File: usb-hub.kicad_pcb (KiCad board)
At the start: 4 copper layers, 50 x 100 mm, 151 parts, among them IC101 USB2517, J101 Barrel_Jack, J102 USB_C_Receptacle_USB2.0_14P, J201 USB_A, J202 USB_A, J301 USB_A, J302 USB_A, J401 USB_A, J402 USB_A, J601 Prog, SW201 SW_Push, SW202 SW_Push, SW301 SW_Push, SW302 SW_Push, SW401 SW_Push, SW402 SW_Push, U101 SRV05-4, U201 MIC2026-1xM, U202 SRV05-4, U203 74LVC2G08, U301 MIC2026-1xM, U302 SRV05-4, U303 74LVC2G08, U401 MIC2026-1xM, U402 SRV05-4, U403 74LVC2G08, U501 TPS54331, U502 TPS54331, U601 STM32L151C8Tx, Y101 24Mhz

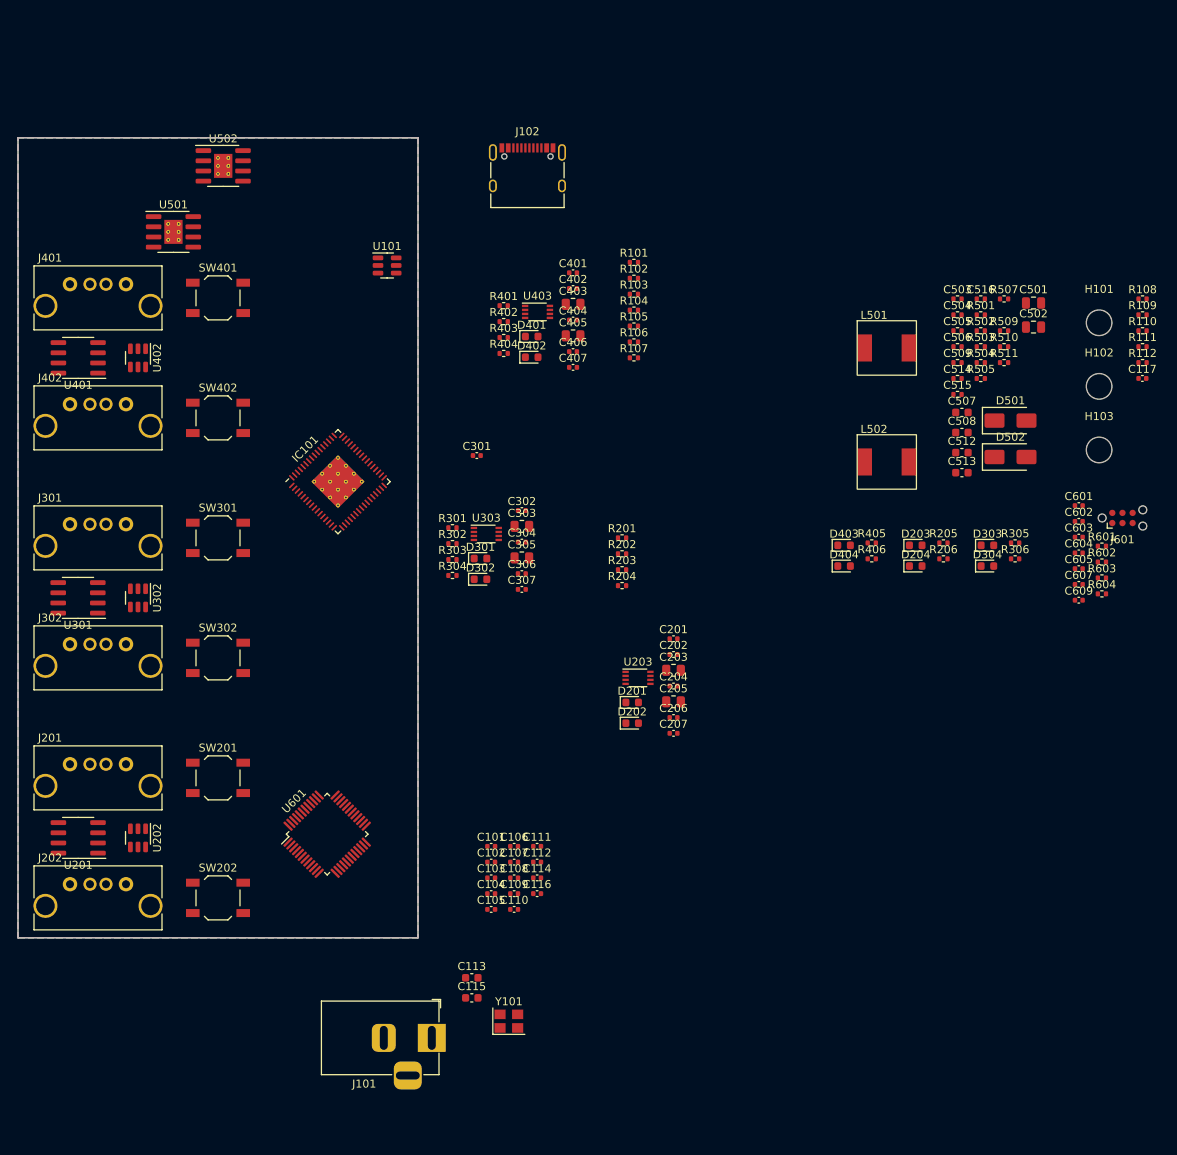
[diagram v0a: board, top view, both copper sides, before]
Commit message: Refine connectors and overall shape
Replace USB connectors, because of availability.
Use available barrel jack and USB-C connector instead of generic ones.
Update 3D Models

Refine rough placement of parts and board outline
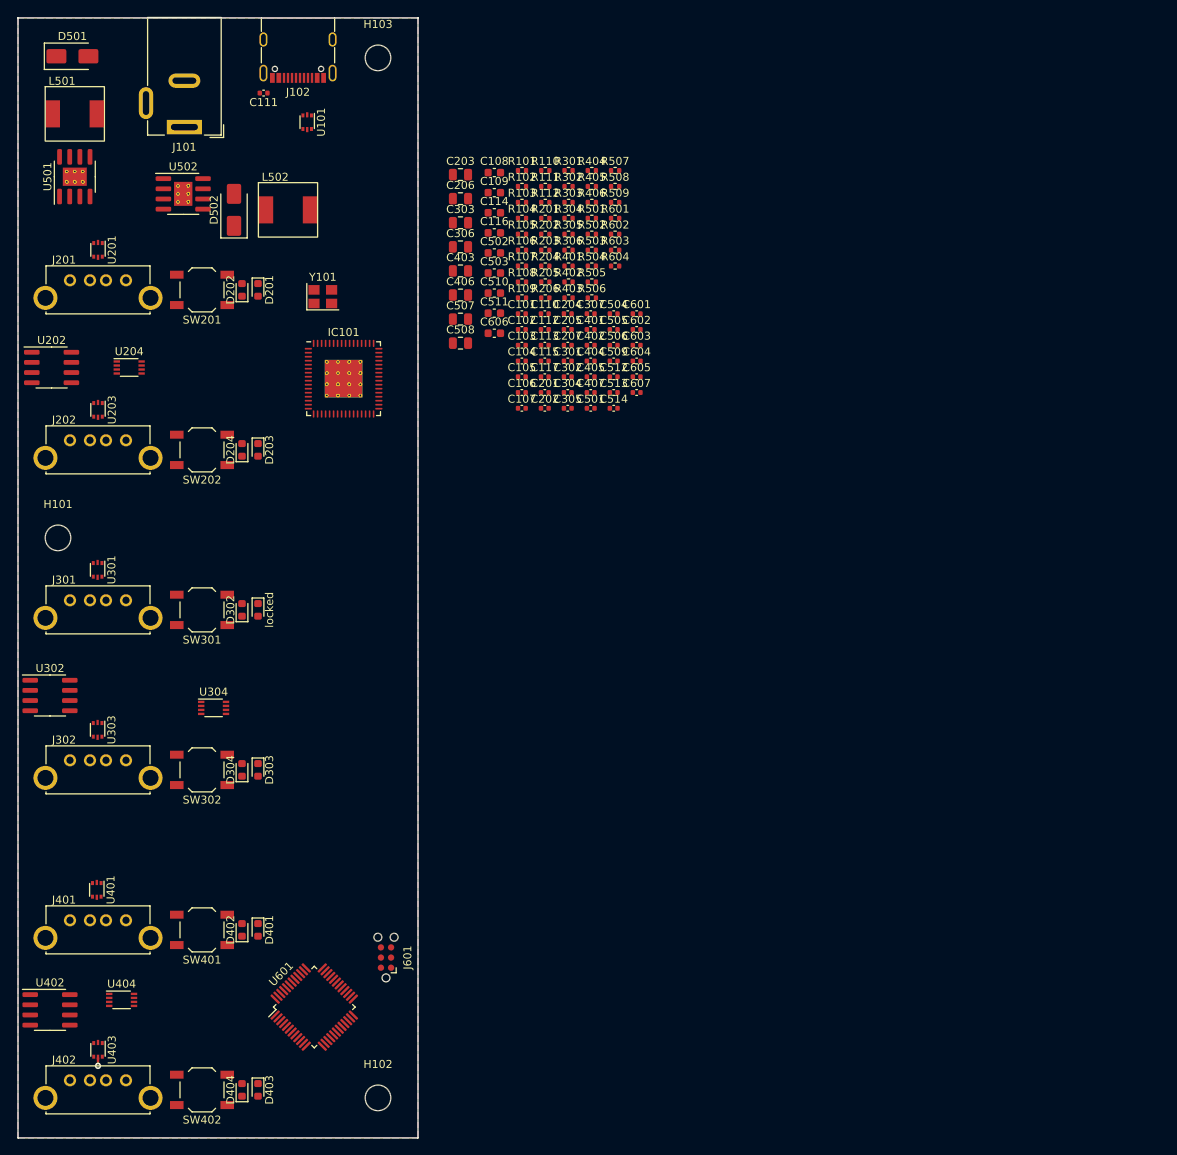
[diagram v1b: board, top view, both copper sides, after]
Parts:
- removed C515: 1nF, Resistor_SMD:R_0402_1005Metric
- removed C516: 47pF, Resistor_SMD:R_0402_1005Metric
- removed C609: 1.0uF, Capacitor_SMD:C_0402_1005Metric
- removed R510: 29,4k, Resistor_SMD:R_0402_1005Metric
- removed R511: 1,5k, Resistor_SMD:R_0402_1005Metric
- added C510: 22uF, Capacitor_SMD:C_0603_1608Metric, F.Cu at (159.5, 69.4)
- added C511: 22uF, Capacitor_SMD:C_0603_1608Metric, F.Cu at (159.5, 71.9)
- added C606: 1.0uF, Capacitor_SMD:C_0603_1608Metric, F.Cu at (159.5, 74.4)
- added R506: 220k, Resistor_SMD:R_0402_1005Metric, F.Cu at (171.7, 70.0)
- added R508: 3,3k, Resistor_SMD:R_0402_1005Metric, F.Cu at (174.6, 56.1)
- added U204: 74LVC2G08, Package_SO:VSSOP-8_2.3x2mm_P0.5mm, F.Cu at (113.9, 78.7)
- added U304: 74LVC2G08, Package_SO:VSSOP-8_2.3x2mm_P0.5mm, F.Cu at (124.5, 121.2)
- added U404: 74LVC2G08, Package_SO:VSSOP-8_2.3x2mm_P0.5mm, F.Cu at (113.0, 157.8)
- C108, C109: footprint Capacitor_SMD:C_0402_1005Metric -> Capacitor_SMD:C_0603_1608Metric
- C111: value C -> 100nF
- C113: value 1.0uF -> C; footprint Capacitor_SMD:C_0603_1608Metric -> Capacitor_SMD:C_0402_1005Metric
- C114, C116: value 100nF -> 1.0uF; footprint Capacitor_SMD:C_0402_1005Metric -> Capacitor_SMD:C_0603_1608Metric
- C115: value 1.0uF -> 100nF; footprint Capacitor_SMD:C_0603_1608Metric -> Capacitor_SMD:C_0402_1005Metric
- C203, C303, C403: footprint Resistor_SMD:R_0805_2012Metric -> Capacitor_SMD:C_0805_2012Metric
- C205, C305, C405: value 47uF -> 100nF; footprint Resistor_SMD:R_0805_2012Metric -> Capacitor_SMD:C_0402_1005Metric
- C206, C306, C406: value 100nF -> 47uF; footprint Capacitor_SMD:C_0402_1005Metric -> Capacitor_SMD:C_0805_2012Metric
- C501: value 10uF -> 100nF; footprint Capacitor_SMD:C_0805_2012Metric -> Capacitor_SMD:C_0402_1005Metric
- C502: value 10uF -> 22uF; footprint Capacitor_SMD:C_0805_2012Metric -> Capacitor_SMD:C_0603_1608Metric
- C503: value 10nF -> 22uF; footprint Resistor_SMD:R_0402_1005Metric -> Capacitor_SMD:C_0603_1608Metric
- C504: value 1nF -> 10nF; footprint Resistor_SMD:R_0402_1005Metric -> Capacitor_SMD:C_0402_1005Metric
- C505: value 47pF -> 1nF; footprint Resistor_SMD:R_0402_1005Metric -> Capacitor_SMD:C_0402_1005Metric
- C506: value 100nF -> 47pF; footprint Resistor_SMD:R_0402_1005Metric -> Capacitor_SMD:C_0402_1005Metric
- C507, C508: value 22uF -> 10uF; footprint Capacitor_SMD:C_0603_1608Metric -> Capacitor_SMD:C_0805_2012Metric
- C509: footprint Resistor_SMD:R_0402_1005Metric -> Capacitor_SMD:C_0402_1005Metric
- C512: value 22uF -> 10nF; footprint Capacitor_SMD:C_0603_1608Metric -> Capacitor_SMD:C_0402_1005Metric
- C513: value 22uF -> 1nF; footprint Capacitor_SMD:C_0603_1608Metric -> Capacitor_SMD:C_0402_1005Metric
- C514: value 10nF -> 47pF; footprint Resistor_SMD:R_0402_1005Metric -> Capacitor_SMD:C_0402_1005Metric
- D201, D203, D303, D401, D403: value LED -> GREEN
- D202, D204, D302, D304, D402, D404: value LED -> BLUE
- J101: value Barrel_Jack -> Barrel_Jack_Switch; footprint Connector_BarrelJack:BarrelJack_Horizontal -> Connector_BarrelJack:BarrelJack_Wuerth_6941xx301002
- J102: footprint Connector_USB:USB_C_Receptacle_XKB_U262-16XN-4BVC11 -> Connector_USB:USB_C_Receptacle_G-Switch_GT-USB-7010ASV
- J201, J202, J301, J302, J401, J402: footprint Connectors:CU01SAV1S00 -> Connectors:UJ2-AV-W4-TH
- R104, R105: value 5.1k -> 100k
- R106: value 1M -> 100k
- R107: value 12k -> 5.1k
- R108: value 100k -> 5.1k
- R110: value 100k -> 1M
- R111: value 100k -> 12k
- R203, R303, R403: value 1k -> 330
- R204, R304, R404: value 100k -> 1k
- R205, R305, R405: value 330 -> 100k
- R501: value 470k -> 10k
- R502: value 220k -> 1,5k
- R503: value 29,4k -> 33k
- R504: value 10k -> 330R
- R505: value 330R -> 470k
- R509: value 3,3k -> 33k
- R602: value 100k -> 10K
- R604: value 10K -> 100k
- U101: value SRV05-4 -> USBLC6-2P6; footprint Package_TO_SOT_SMD:SOT-23-6 -> Package_TO_SOT_SMD:SOT-666
- U201, U301, U401: value MIC2026-1xM -> USBLC6-2P6; footprint Package_SO:SOIC-8_3.9x4.9mm_P1.27mm -> Package_TO_SOT_SMD:SOT-666
- U202, U302, U402: value SRV05-4 -> MIC2026-1xM; footprint Package_TO_SOT_SMD:SOT-23-6 -> Package_SO:SOIC-8_3.9x4.9mm_P1.27mm
- U203, U303, U403: value 74LVC2G08 -> USBLC6-2P6; footprint Package_SO:VSSOP-8_2.3x2mm_P0.5mm -> Package_TO_SOT_SMD:SOT-666
- locked: renamed from D301; value LED -> GREEN
- moved H101 132.9 mm to (105.0, 100.0)
- moved H102 126.6 mm to (145.0, 170.0)
- moved D501 125.8 mm to (106.8, 39.8)
- moved J101 118.0 mm to (120.8, 48.6), turned to 180 degrees
- moved U403 107.4 mm to (110.0, 164.0), turned to -90 degrees
- moved J601 107.2 mm to (146.0, 152.5), turned to 90 degrees
- moved L501 105.6 mm to (107.1, 47.0)
- moved H103 102.6 mm to (145.0, 40.0)
- moved D502 101.9 mm to (127.0, 59.0), turned to 90 degrees
- moved C111 100.2 mm to (130.7, 44.4), turned to 180 degrees
- moved D403 100.0 mm to (130.0, 169.0), turned to -90 degrees
- moved D404 99.8 mm to (128.0, 169.0), turned to 90 degrees
- moved D304 96.6 mm to (128.0, 129.0), turned to 90 degrees
- moved D303 95.4 mm to (130.0, 129.0), turned to -90 degrees
- moved Y101 93.5 mm to (138.1, 69.8)
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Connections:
- C111 pad 1: /XTAL_IN -> GND
- C111 pad 2: GND -> Earth
- C112 pad 1: /XTAL_OUT -> /XTAL_IN
- C113 pad 1: Net-(IC101-VDD18) -> /XTAL_OUT
- C115 pad 1: Net-(IC101-VDD18PLL) -> Net-(IC101-VDD18)
- C117 pad 1: GND -> Net-(IC101-VDD18PLL)
- C117 pad 2: Earth -> GND
- C204 pad 1: /Port 1-2/VBUS_B -> GND
- C204 pad 2: GND -> Earth
- C206 pad 1: GND -> /Port 1-2/VBUS_B
- C206 pad 2: Earth -> GND
- C304 pad 1: /Port 3-4/VBUS_B -> GND
- C304 pad 2: GND -> Earth
- C306 pad 1: GND -> /Port 3-4/VBUS_B
- C306 pad 2: Earth -> GND
- C404 pad 1: /Port 5-6/VBUS_B -> GND
- C404 pad 2: GND -> Earth
- C406 pad 1: GND -> /Port 5-6/VBUS_B
- C406 pad 2: Earth -> GND
- C501 pad 1: /Power/3.5-28V -> Net-(U501-BOOT)
- C501 pad 2: GND -> Net-(D501-K)
- C502 pad 1: /Power/3.5-28V -> +5V
- C503 pad 1: Net-(U501-SS) -> +5V
- C504 pad 1: Net-(U501-COMP) -> Net-(U501-SS)
- C504 pad 2: Net-(C504-Pad2) -> GND
- C505 pad 2: GND -> Net-(C505-Pad2)
- C506 pad 1: Net-(U501-BOOT) -> Net-(U501-COMP)
- C506 pad 2: Net-(D501-K) -> GND
- C507 pad 1: +5V -> /Power/3.5-28V
- C508 pad 1: +5V -> /Power/3.5-28V
- C512 pad 1: +3V3 -> Net-(U502-SS)
- C513 pad 1: +3V3 -> Net-(U502-COMP)
- C513 pad 2: GND -> Net-(C513-Pad2)
- C514 pad 1: Net-(U502-SS) -> Net-(U502-COMP)
- D201 pad 1: GND -> Net-(D201-K)
- D201 pad 2: Net-(D201-A) -> +3V3
- D204 pad 1: Net-(D204-K) -> GND
- D204 pad 2: +3V3 -> Net-(D204-A)
- D304 pad 1: Net-(D304-K) -> GND
- D304 pad 2: +3V3 -> Net-(D304-A)
- D401 pad 1: GND -> Net-(D401-K)
- D401 pad 2: Net-(D401-A) -> +3V3
- D404 pad 1: Net-(D404-K) -> GND
- D404 pad 2: +3V3 -> Net-(D404-A)
- IC101 pad 58: Net-(IC101-USBUP_DM) -> /USB_UP_D-
- IC101 pad 59: Net-(IC101-USBUP_DP) -> /USB_UP_D+
- J101 pad 3: (no net) -> GND
- J102 pad A4: Net-(U101-VP) -> Net-(U101-VBUS)
- J102 pad A6: Net-(IC101-USBUP_DP) -> /USB_UP_UNSCHIELDED_D+
- J102 pad A7: Net-(IC101-USBUP_DM) -> /USB_UP_UNSCHIELDED_D-
- J102 pad A9: Net-(U101-VP) -> Net-(U101-VBUS)
- J102 pad B4: Net-(U101-VP) -> Net-(U101-VBUS)
- J102 pad B6: Net-(IC101-USBUP_DP) -> /USB_UP_UNSCHIELDED_D+
- J102 pad B7: Net-(IC101-USBUP_DM) -> /USB_UP_UNSCHIELDED_D-
- J102 pad B9: Net-(U101-VP) -> Net-(U101-VBUS)
- J201 pad 2: /Port 1-2/USB_A_D- -> /Port 1-2/USB_A_UNSCHIELDED_D-
- J201 pad 3: /Port 1-2/USB_A_D+ -> /Port 1-2/USB_A_UNSCHIELDED_D+
- J202 pad 2: /Port 1-2/USB_B_D- -> /Port 1-2/USB_B_UNSCHIELDED_D-
- J202 pad 3: /Port 1-2/USB_B_D+ -> /Port 1-2/USB_B_UNSCHIELDED_D+
- J301 pad 2: /Port 3-4/USB_A_D- -> /Port 3-4/USB_A_UNSCHIELDED_D-
- J301 pad 3: /Port 3-4/USB_A_D+ -> /Port 3-4/USB_A_UNSCHIELDED_D+
- J302 pad 2: /Port 3-4/USB_B_D- -> /Port 3-4/USB_B_UNSCHIELDED_D-
- J302 pad 3: /Port 3-4/USB_B_D+ -> /Port 3-4/USB_B_UNSCHIELDED_D+
- J401 pad 2: /Port 5-6/USB_A_D- -> /Port 5-6/USB_A_UNSCHIELDED_D-
- J401 pad 3: /Port 5-6/USB_A_D+ -> /Port 5-6/USB_A_UNSCHIELDED_D+
- J402 pad 2: /Port 5-6/USB_B_D- -> /Port 5-6/USB_B_UNSCHIELDED_D-
- J402 pad 3: /Port 5-6/USB_B_D+ -> /Port 5-6/USB_B_UNSCHIELDED_D+
- R102 pad 1: Net-(U101-VP) -> Net-(IC101-LED_B1_N/BOOST0)
- R102 pad 2: /VBUS_DET -> GND
- R103 pad 1: /VBUS_DET -> Net-(U101-VBUS)
- R103 pad 2: GND -> /VBUS_DET
- R104 pad 1: Net-(J102-CC2) -> /VBUS_DET
- R105 pad 1: Net-(J102-CC1) -> Net-(IC101-LED_B2_N/BOOST1)
- R106 pad 1: /XTAL_IN -> Net-(IC101-LED_B3_N/GANG_EN)
- R106 pad 2: /XTAL_OUT -> GND
- R107 pad 1: GND -> Net-(J102-CC2)
- R107 pad 2: Net-(IC101-RBIAS) -> GND
- R108 pad 1: Net-(IC101-LED_A7_N/PRT_SWP7) -> Net-(J102-CC1)
- R110 pad 1: Net-(IC101-LED_B3_N/GANG_EN) -> /XTAL_IN
- R110 pad 2: GND -> /XTAL_OUT
- R111 pad 1: Net-(IC101-LED_B2_N/BOOST1) -> GND
- R111 pad 2: GND -> Net-(IC101-RBIAS)
- R112 pad 1: Net-(IC101-LED_B1_N/BOOST0) -> Net-(IC101-LED_A7_N/PRT_SWP7)
- R201 pad 2: Net-(D201-A) -> Net-(D202-A)
- R203 pad 1: /Port 1-2/VBUS_B -> Net-(D201-K)
- R203 pad 2: Net-(D202-A) -> /Port 1-2/LED_IND_A
- R204 pad 1: +3V3 -> /Port 1-2/VBUS_B
- R204 pad 2: /Port 1-2/PORT_B_REQ -> Net-(D204-A)
- R205 pad 1: Net-(D203-K) -> +3V3
- R205 pad 2: /Port 1-2/LED_IND_A -> /Port 1-2/PORT_B_REQ
- R206 pad 1: Net-(D204-K) -> Net-(D203-K)
- R301 pad 2: Net-(D301-A) -> Net-(D302-A)
- R303 pad 1: /Port 3-4/VBUS_B -> Net-(D301-K)
- R303 pad 2: Net-(D302-A) -> /Port 3-4/LED_IND_A
- R304 pad 1: +3V3 -> /Port 3-4/VBUS_B
- R304 pad 2: /Port 3-4/PORT_B_REQ -> Net-(D304-A)
- R305 pad 1: Net-(D303-K) -> +3V3
- R305 pad 2: /Port 3-4/LED_IND_A -> /Port 3-4/PORT_B_REQ
- R306 pad 1: Net-(D304-K) -> Net-(D303-K)
- R401 pad 2: Net-(D401-A) -> Net-(D402-A)
- R403 pad 1: /Port 5-6/VBUS_B -> Net-(D401-K)
- R403 pad 2: Net-(D402-A) -> /Port 5-6/LED_IND_A
- R404 pad 1: +3V3 -> /Port 5-6/VBUS_B
- R404 pad 2: /Port 5-6/PORT_B_REQ -> Net-(D404-A)
- R405 pad 1: Net-(D403-K) -> +3V3
- R405 pad 2: /Port 5-6/LED_IND_A -> /Port 5-6/PORT_B_REQ
- R406 pad 1: Net-(D404-K) -> Net-(D403-K)
- R501 pad 1: /Power/3.5-28V -> +5V
- R501 pad 2: /Power/POWER_ENABLE -> /Power/VSENSE_5V
- R502 pad 1: /Power/POWER_ENABLE -> /Power/VSENSE_5V
- R502 pad 2: GND -> Net-(R502-Pad2)
- R503 pad 1: Net-(C504-Pad2) -> Net-(C505-Pad2)
- R504 pad 1: +5V -> Net-(R502-Pad2)
- R504 pad 2: /Power/VSENSE_5V -> GND
- R505 pad 1: Net-(R505-Pad1) -> /Power/3.5-28V
- R505 pad 2: GND -> /Power/POWER_ENABLE
- R509 pad 1: /Power/VSENSE_3V -> Net-(C513-Pad2)
- R602 pad 2: /Power controller/RESET_N -> /SCL
- R604 pad 2: /SCL -> /Power controller/RESET_N
- U101 pad 1: Net-(IC101-USBUP_DP) -> /USB_UP_UNSCHIELDED_D-
- U101 pad 3: Net-(IC101-USBUP_DM) -> /USB_UP_UNSCHIELDED_D+
- U101 pad 4: unconnected-(U101-IO3-Pad4) -> /USB_UP_D+
- U101 pad 5: Net-(U101-VP) -> Net-(U101-VBUS)
- U101 pad 6: unconnected-(U101-IO4-Pad6) -> /USB_UP_D-
- U201 pad 1: /Port 1-2/PORT_A_EN -> /Port 1-2/USB_A_D+
- U201 pad 2: /Port 1-2/PORT_A_OC -> GND
- U201 pad 3: /Port 1-2/PORT_B_OC -> /Port 1-2/USB_A_D-
- U201 pad 4: /Port 1-2/PORT_B_EN -> /Port 1-2/USB_A_UNSCHIELDED_D-
- U201 pad 5: /Port 1-2/VBUS_B -> +5V
- U201 pad 6: GND -> /Port 1-2/USB_A_UNSCHIELDED_D+
- U202 pad 1: /Port 1-2/USB_A_D+ -> /Port 1-2/PORT_A_EN
- U202 pad 2: GND -> /Port 1-2/PORT_A_OC
- U202 pad 3: /Port 1-2/USB_A_D- -> /Port 1-2/PORT_B_OC
- U202 pad 4: /Port 1-2/USB_B_D- -> /Port 1-2/PORT_B_EN
- U202 pad 5: +5V -> /Port 1-2/VBUS_B
- U202 pad 6: /Port 1-2/USB_B_D+ -> GND
- U203 pad 1: /Port 1-2/PORT_A_EN_1 -> /Port 1-2/USB_B_D+
- U203 pad 2: /Port 1-2/PORT_A_EN_2 -> GND
- U203 pad 3: /Port 1-2/PORT_B_EN -> /Port 1-2/USB_B_D-
- U203 pad 4: GND -> /Port 1-2/USB_B_UNSCHIELDED_D-
- U203 pad 5: /Port 1-2/PORT_B_EN_1 -> +5V
- U203 pad 6: /Port 1-2/PORT_B_EN_2 -> /Port 1-2/USB_B_UNSCHIELDED_D+
- U301 pad 1: /Port 3-4/PORT_A_EN -> /Port 3-4/USB_A_D+
- U301 pad 2: /Port 3-4/PORT_A_OC -> GND
- U301 pad 3: /Port 3-4/PORT_B_OC -> /Port 3-4/USB_A_D-
- U301 pad 4: /Port 3-4/PORT_B_EN -> /Port 3-4/USB_A_UNSCHIELDED_D-
- U301 pad 5: /Port 3-4/VBUS_B -> +5V
- U301 pad 6: GND -> /Port 3-4/USB_A_UNSCHIELDED_D+
- U302 pad 1: /Port 3-4/USB_A_D+ -> /Port 3-4/PORT_A_EN
- U302 pad 2: GND -> /Port 3-4/PORT_A_OC
- U302 pad 3: /Port 3-4/USB_A_D- -> /Port 3-4/PORT_B_OC
- U302 pad 4: /Port 3-4/USB_B_D- -> /Port 3-4/PORT_B_EN
- U302 pad 5: +5V -> /Port 3-4/VBUS_B
- U302 pad 6: /Port 3-4/USB_B_D+ -> GND
- U303 pad 1: /Port 3-4/PORT_A_EN_1 -> /Port 3-4/USB_B_D+
- U303 pad 2: /Port 3-4/PORT_A_EN_2 -> GND
- U303 pad 3: /Port 3-4/PORT_B_EN -> /Port 3-4/USB_B_D-
- U303 pad 4: GND -> /Port 3-4/USB_B_UNSCHIELDED_D-
- U303 pad 5: /Port 3-4/PORT_B_EN_1 -> +5V
- U303 pad 6: /Port 3-4/PORT_B_EN_2 -> /Port 3-4/USB_B_UNSCHIELDED_D+
- U401 pad 1: /Port 5-6/PORT_A_EN -> /Port 5-6/USB_A_D+
- U401 pad 2: /Port 5-6/PORT_A_OC -> GND
- U401 pad 3: /Port 5-6/PORT_B_OC -> /Port 5-6/USB_A_D-
- U401 pad 4: /Port 5-6/PORT_B_EN -> /Port 5-6/USB_A_UNSCHIELDED_D-
- U401 pad 5: /Port 5-6/VBUS_B -> +5V
- U401 pad 6: GND -> /Port 5-6/USB_A_UNSCHIELDED_D+
- U402 pad 1: /Port 5-6/USB_A_D+ -> /Port 5-6/PORT_A_EN
- U402 pad 2: GND -> /Port 5-6/PORT_A_OC
- U402 pad 3: /Port 5-6/USB_A_D- -> /Port 5-6/PORT_B_OC
- U402 pad 4: /Port 5-6/USB_B_D- -> /Port 5-6/PORT_B_EN
- U402 pad 5: +5V -> /Port 5-6/VBUS_B
- U402 pad 6: /Port 5-6/USB_B_D+ -> GND
- U403 pad 1: /Port 5-6/PORT_A_EN_1 -> /Port 5-6/USB_B_D+
- U403 pad 2: /Port 5-6/PORT_A_EN_2 -> GND
- U403 pad 3: /Port 5-6/PORT_B_EN -> /Port 5-6/USB_B_D-
- U403 pad 4: GND -> /Port 5-6/USB_B_UNSCHIELDED_D-
- U403 pad 5: /Port 5-6/PORT_B_EN_1 -> +5V
- U403 pad 6: /Port 5-6/PORT_B_EN_2 -> /Port 5-6/USB_B_UNSCHIELDED_D+
- locked pad 1: GND -> Net-(D301-K)
- locked pad 2: Net-(D301-A) -> +3V3
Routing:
- net +5V: track 0.00 -> 1.07 mm, vias 0 -> 1
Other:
- board size 50 x 100 mm -> 50 x 140 mm

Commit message: Add preliminary routing
Add routing for power paths - 3.3V, 5V and Input power

Add routing close to USB-Ports

Mising routing for main IC's and differntial pair routing
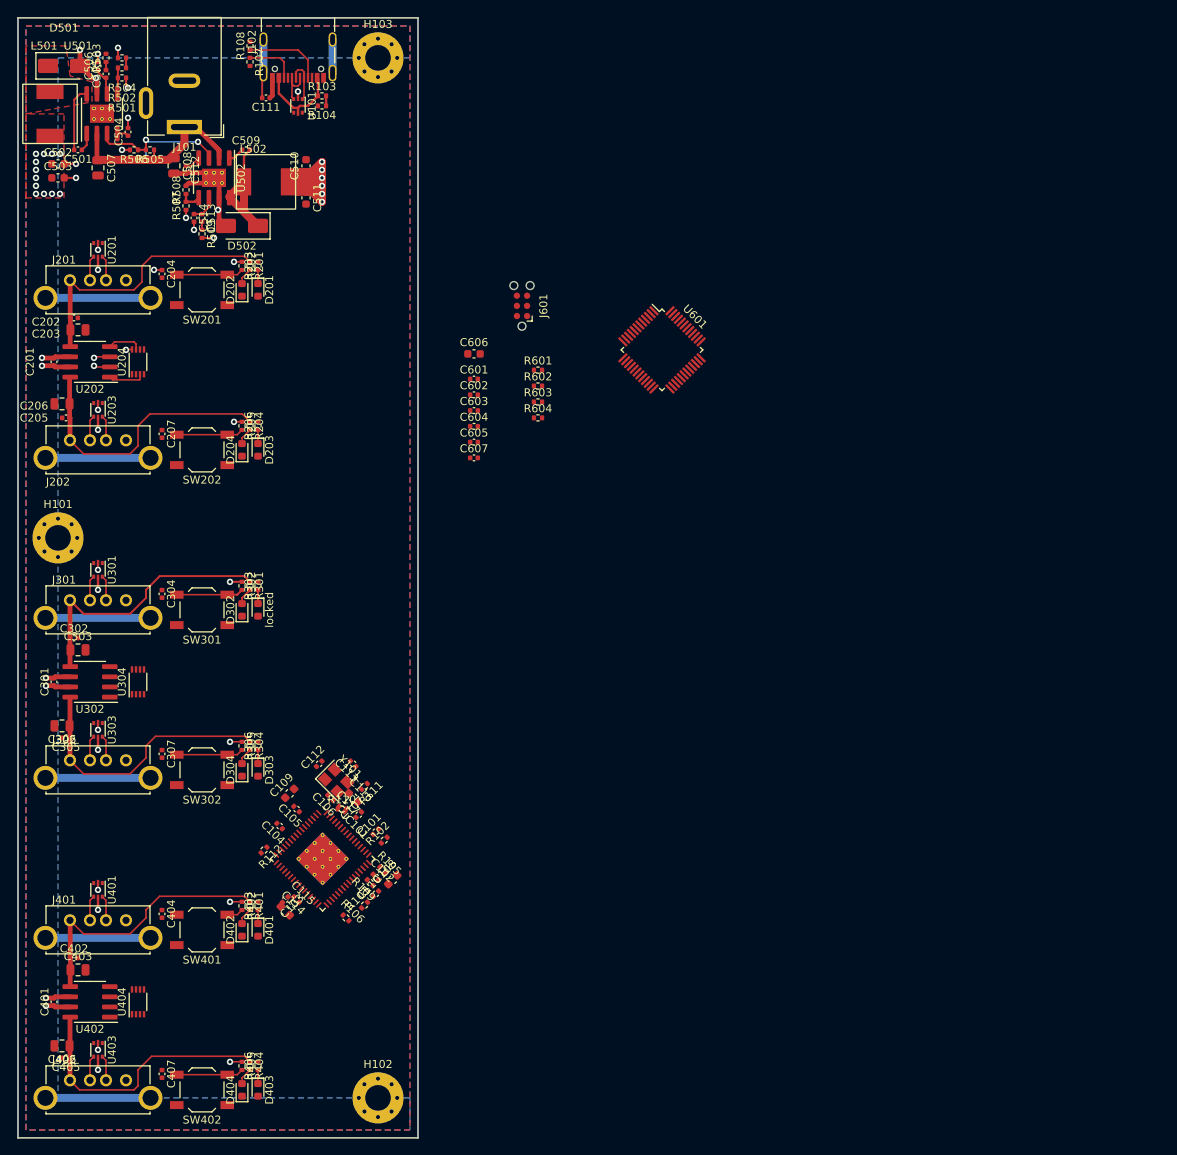
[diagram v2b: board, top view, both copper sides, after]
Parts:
- H101, H102, H103: footprint MountingHole:MountingHole_3.2mm_M3 -> MountingHole:MountingHole_3.2mm_M3_Pad_Via
- moved R404 119.8 mm to (129.0, 166.0), turned to -90 degrees
- moved R405 118.3 mm to (128.0, 166.0), turned to -90 degrees
- moved R406 115.7 mm to (130.0, 166.0), turned to 90 degrees
- moved C401 107.5 mm to (104.5, 158.0), turned to 90 degrees
- moved C405 107.5 mm to (106.0, 165.0), turned to 180 degrees
- moved C406 106.3 mm to (105.5, 163.5), turned to 180 degrees
- moved C407 100.6 mm to (118.0, 167.0), turned to -90 degrees
- moved C402 100.2 mm to (107.0, 152.5)
- moved C403 99.6 mm to (107.5, 154.0)
- moved R101 93.9 mm to (143.3, 145.9), turned to 45 degrees
- moved U601 92.9 mm to (180.5, 76.5), turned to -45 degrees
- moved C114 91.1 mm to (133.4, 146.6), turned to -45 degrees
- moved R401 89.3 mm to (129.0, 146.0), turned to -90 degrees
- moved C108 89.3 mm to (146.8, 142.7), turned to 45 degrees
- moved R112 88.3 mm to (130.8, 139.0), turned to -135 degrees
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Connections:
- net Net-(U101-VBUS) renamed /USB_VBUS
- U202 pad 1: /Port 1-2/PORT_A_EN -> /Port 1-2/PORT_B_EN
- U202 pad 2: /Port 1-2/PORT_A_OC -> /Port 1-2/PORT_B_OC
- U202 pad 3: /Port 1-2/PORT_B_OC -> /Port 1-2/PORT_A_OC
- U202 pad 4: /Port 1-2/PORT_B_EN -> /Port 1-2/PORT_A_EN
- U202 pad 5: /Port 1-2/VBUS_B -> /Port 1-2/VBUS_A
- U202 pad 8: /Port 1-2/VBUS_A -> /Port 1-2/VBUS_B
- U302 pad 1: /Port 3-4/PORT_A_EN -> /Port 3-4/PORT_B_EN
- U302 pad 2: /Port 3-4/PORT_A_OC -> /Port 3-4/PORT_B_OC
- U302 pad 3: /Port 3-4/PORT_B_OC -> /Port 3-4/PORT_A_OC
- U302 pad 4: /Port 3-4/PORT_B_EN -> /Port 3-4/PORT_A_EN
- U302 pad 5: /Port 3-4/VBUS_B -> /Port 3-4/VBUS_A
- U302 pad 8: /Port 3-4/VBUS_A -> /Port 3-4/VBUS_B
- U402 pad 1: /Port 5-6/PORT_A_EN -> /Port 5-6/PORT_B_EN
- U402 pad 2: /Port 5-6/PORT_A_OC -> /Port 5-6/PORT_B_OC
- U402 pad 3: /Port 5-6/PORT_B_OC -> /Port 5-6/PORT_A_OC
- U402 pad 4: /Port 5-6/PORT_B_EN -> /Port 5-6/PORT_A_EN
- U402 pad 5: /Port 5-6/VBUS_B -> /Port 5-6/VBUS_A
- U402 pad 8: /Port 5-6/VBUS_A -> /Port 5-6/VBUS_B
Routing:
- net (no net): track 0.00 -> 78.8 mm
- net GND: track 0.00 -> 50.0 mm, vias 0 -> 22
- net +3V3: track 0.00 -> 38.9 mm, vias 0 -> 14
- net /Port 1-2/VBUS_B: track 0.00 -> 35.1 mm
- net /Port 1-2/VBUS_A: track 0.00 -> 34.5 mm
- net /Port 3-4/VBUS_A: track 0.00 -> 34.3 mm
- net /Port 5-6/VBUS_A: track 0.00 -> 34.3 mm
- net /Port 3-4/VBUS_B: track 0.00 -> 34.2 mm
- net /Port 5-6/VBUS_B: track 0.00 -> 34.1 mm
- net /Power/3.5-28V: track 0.00 -> 26.1 mm
- net +5V: track 1.07 -> 20.6 mm, vias 1 -> 22
- net /Power/POWER_ENABLE: track 0.00 -> 19.5 mm, vias 0 -> 2
- net Net-(D502-K): track 0.00 -> 18.3 mm
- net Earth: track 0.00 -> 11.6 mm
- net /USB_VBUS: track 0.00 -> 11.2 mm
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- added copper zone on In2.Cu, net +3V3
- added copper zone on F.Cu, net +5V
- added copper zone on In2.Cu, net +5V
- added copper zone on B.Cu, net Earth
- added copper zone on F.Cu, net Net-(D501-K)
- removed copper zone on In2.Cu, net GND
